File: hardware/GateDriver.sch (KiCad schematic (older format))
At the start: 9 parts

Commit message: updated routing and all plots
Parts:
- C1, C2, C3: value 0.1u -> 0.68u; PN GCM21BR72A104KA37K -> CGA4J3X7R1H684K125AB
- PhaseA1, PhaseB1, PhaseC1: value UCC2720xA -> UCC27211A
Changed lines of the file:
@@
 P 3800 1900
 F 0 "PhaseA1" H 3900 1500 60  0000 C CNN
-F 1 "UCC2720xA" H 3900 2100 60  0000 C CNN
+F 1 "UCC27211A" H 3900 2100 60  0000 C CNN
 F 2 "Housings_SOIC:Infineon_PG-DSO-8-43" H 3800 1900 60  0001 C CNN
 F 3 "" H 3800 1900 60  0001 C CNN
@@
 P 3800 3000
 F 0 "PhaseB1" H 3900 2600 60  0000 C CNN
-F 1 "UCC2720xA" H 3900 3200 60  0000 C CNN
+F 1 "UCC27211A" H 3900 3200 60  0000 C CNN
 F 2 "Housings_SOIC:Infineon_PG-DSO-8-43" H 3800 3000 60  0001 C CNN
 F 3 "" H 3800 3000 60  0001 C CNN
@@
 P 3800 4150
 F 0 "PhaseC1" H 3900 3750 60  0000 C CNN
-F 1 "UCC2720xA" H 3900 4350 60  0000 C CNN
+F 1 "UCC27211A" H 3900 4350 60  0000 C CNN
 F 2 "Housings_SOIC:Infineon_PG-DSO-8-43" H 3800 4150 60  0001 C CNN
 F 3 "" H 3800 4150 60  0001 C CNN
@@
 P 2450 2100
 F 0 "C3" H 2475 2200 50  0000 L CNN
-F 1 "0.1u" H 2475 2000 50  0000 L CNN
+F 1 "0.68u" H 2475 2000 50  0000 L CNN
 F 2 "Capacitors_SMD:C_0805_HandSoldering" H 2488 1950 50  0001 C CNN
 F 3 "" H 2450 2100 50  0001 C CNN
-F 4 "GCM21BR72A104KA37K" H 1800 2100 60  0000 C CNN "PN"
+F 4 "CGA4J3X7R1H684K125AB" H 1800 2100 60  0000 C CNN "PN"
 	1    2450 2100
 	1    0    0    -1
@@
 P 2400 3200
 F 0 "C1" H 2425 3300 50  0000 L CNN
-F 1 "0.1u" H 2425 3100 50  0000 L CNN
+F 1 "0.68u" H 2425 3100 50  0000 L CNN
 F 2 "Capacitors_SMD:C_0805_HandSoldering" H 2438 3050 50  0001 C CNN
 F 3 "" H 2400 3200 50  0001 C CNN
-F 4 "GCM21BR72A104KA37K" H 1750 3200 60  0000 C CNN "PN"
+F 4 "CGA4J3X7R1H684K125AB" H 1750 3200 60  0000 C CNN "PN"
 	1    2400 3200
 	1    0    0    -1
@@
 P 2400 4350
 F 0 "C2" H 2425 4450 50  0000 L CNN
-F 1 "0.1u" H 2425 4250 50  0000 L CNN
+F 1 "0.68u" H 2425 4250 50  0000 L CNN
 F 2 "Capacitors_SMD:C_0805_HandSoldering" H 2438 4200 50  0001 C CNN
 F 3 "" H 2400 4350 50  0001 C CNN
-F 4 "GCM21BR72A104KA37K" H 1750 4350 60  0000 C CNN "PN"
+F 4 "CGA4J3X7R1H684K125AB" H 1750 4350 60  0000 C CNN "PN"
 	1    2400 4350
 	1    0    0    -1

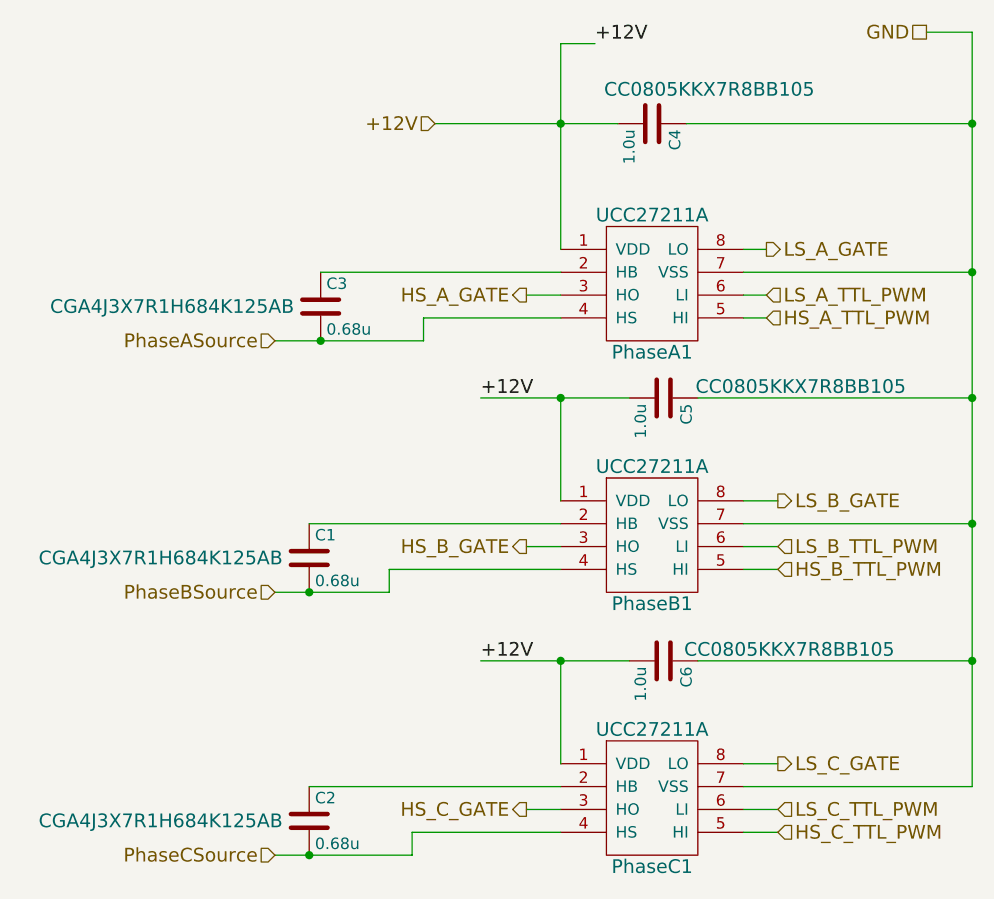
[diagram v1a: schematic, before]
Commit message: Updated schematic for additional capacitors
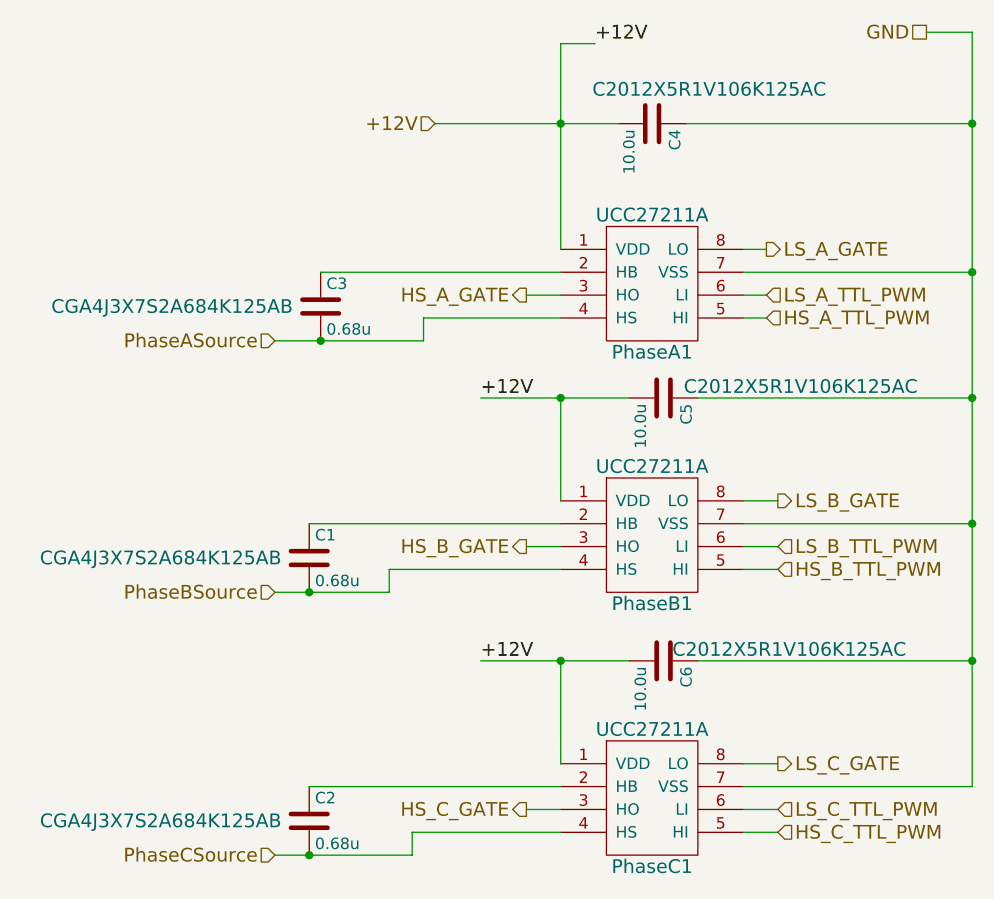
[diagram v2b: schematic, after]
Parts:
- C1, C2, C3: PN CGA4J3X7R1H684K125AB -> CGA4J3X7S2A684K125AB
- C4, C5, C6: value 1.0u -> 10.0u; PN CC0805KKX7R8BB105 -> C2012X5R1V106K125AC
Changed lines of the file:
@@
 F 2 "Capacitors_SMD:C_0805_HandSoldering" H 2488 1950 50  0001 C CNN
 F 3 "" H 2450 2100 50  0001 C CNN
-F 4 "CGA4J3X7R1H684K125AB" H 1800 2100 60  0000 C CNN "PN"
+F 4 "CGA4J3X7S2A684K125AB" H 1800 2100 60  0000 C CNN "PN"
 	1    2450 2100
 	1    0    0    -1
@@
 F 2 "Capacitors_SMD:C_0805_HandSoldering" H 2438 3050 50  0001 C CNN
 F 3 "" H 2400 3200 50  0001 C CNN
-F 4 "CGA4J3X7R1H684K125AB" H 1750 3200 60  0000 C CNN "PN"
+F 4 "CGA4J3X7S2A684K125AB" H 1750 3200 60  0000 C CNN "PN"
 	1    2400 3200
 	1    0    0    -1
@@
 F 2 "Capacitors_SMD:C_0805_HandSoldering" H 2438 4200 50  0001 C CNN
 F 3 "" H 2400 4350 50  0001 C CNN
-F 4 "CGA4J3X7R1H684K125AB" H 1750 4350 60  0000 C CNN "PN"
+F 4 "CGA4J3X7S2A684K125AB" H 1750 4350 60  0000 C CNN "PN"
 	1    2400 4350
 	1    0    0    -1
@@
 P 3900 1300
 F 0 "C4" H 3925 1400 50  0000 L CNN
-F 1 "1.0u" H 3925 1200 50  0000 L CNN
+F 1 "10.0u" H 3925 1200 50  0000 L CNN
 F 2 "Capacitors_SMD:C_0805_HandSoldering" H 3938 1150 50  0001 C CNN
 F 3 "" H 3900 1300 50  0001 C CNN
-F 4 "CC0805KKX7R8BB105 " V 3750 1550 60  0000 C CNN "PN"
+F 4 "C2012X5R1V106K125AC" V 3750 1550 60  0000 C CNN "PN"
 	1    3900 1300
 	0    1    1    0
@@
 P 3950 2500
 F 0 "C5" H 3975 2600 50  0000 L CNN
-F 1 "1.0u" H 3975 2400 50  0000 L CNN
+F 1 "10.0u" H 3975 2400 50  0000 L CNN
 F 2 "Capacitors_SMD:C_0805_HandSoldering" H 3988 2350 50  0001 C CNN
 F 3 "" H 3950 2500 50  0001 C CNN
-F 4 "CC0805KKX7R8BB105 " V 3900 3100 60  0000 C CNN "PN"
+F 4 "C2012X5R1V106K125AC" V 3900 3100 60  0000 C CNN "PN"
 	1    3950 2500
 	0    1    1    0
@@
 P 3950 3650
 F 0 "C6" H 3975 3750 50  0000 L CNN
-F 1 "1.0u" H 3975 3550 50  0000 L CNN
+F 1 "10.0u" H 3975 3550 50  0000 L CNN
 F 2 "Capacitors_SMD:C_0805_HandSoldering" H 3988 3500 50  0001 C CNN
 F 3 "" H 3950 3650 50  0001 C CNN
-F 4 "CC0805KKX7R8BB105 " V 3900 4200 60  0000 C CNN "PN"
+F 4 "C2012X5R1V106K125AC" V 3900 4200 60  0000 C CNN "PN"
 	1    3950 3650
 	0    1    1    0
